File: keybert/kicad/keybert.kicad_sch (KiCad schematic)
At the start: 52 parts, among them SW0 MX-NoLED, SW1 MX-NoLED, SW10 MX-NoLED, SW11 MX-NoLED, SW12 MX-NoLED, SW13 MX-NoLED, SW14 MX-NoLED, SW15 MX-NoLED, SW16 MX-NoLED, SW17 MX-NoLED, SW18 MX-NoLED, SW19 MX-NoLED, SW2 MX-NoLED, SW20 MX-NoLED, SW21 MX-NoLED, SW22 MX-NoLED, SW3 MX-NoLED, SW4 MX-NoLED, SW5 MX-NoLED, SW6 MX-NoLED, SW7 MX-NoLED, SW8 MX-NoLED, SW9 MX-NoLED, U0 ProMicro

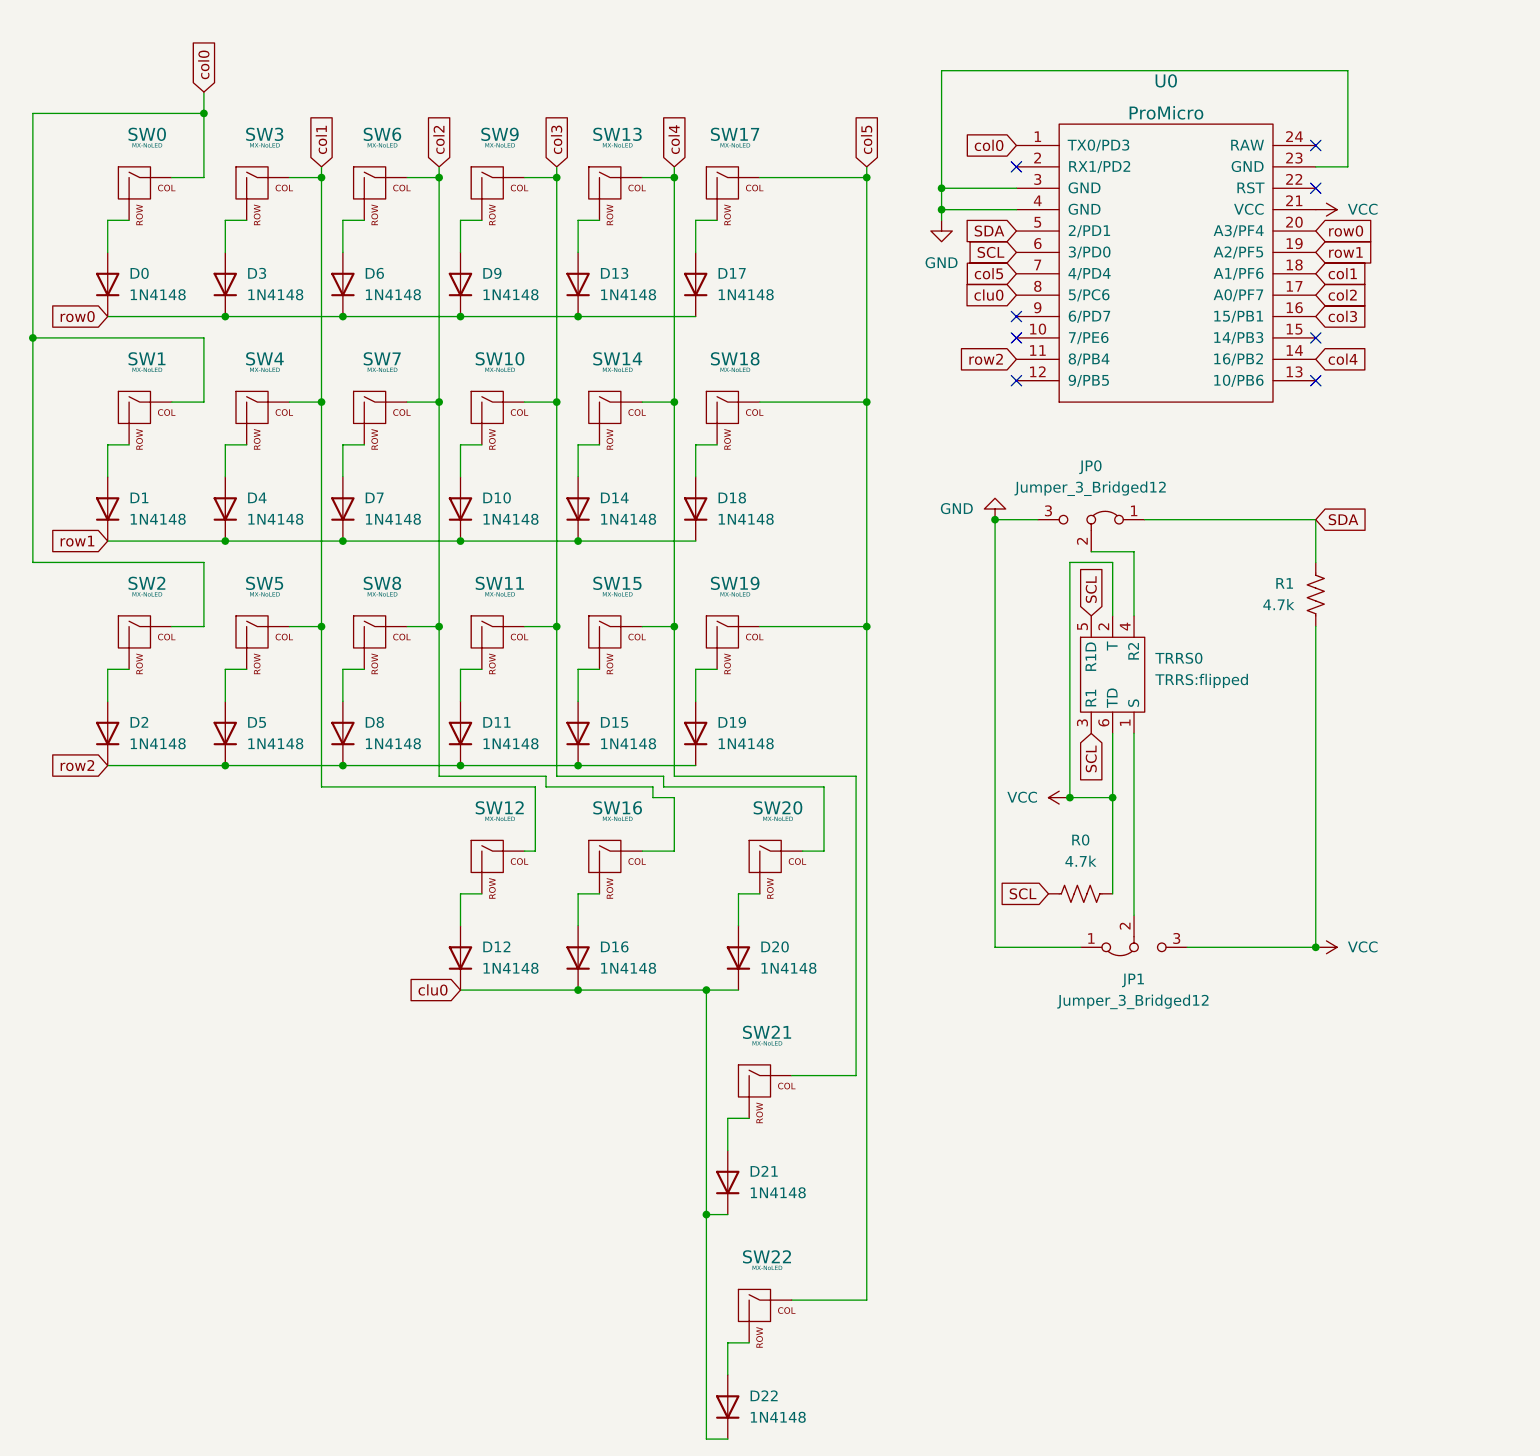
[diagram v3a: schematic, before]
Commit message: feat: remade parametric model of switch plate
I'm going to have a friend help me get it sorted out why the parameters
are coming out so under constrained
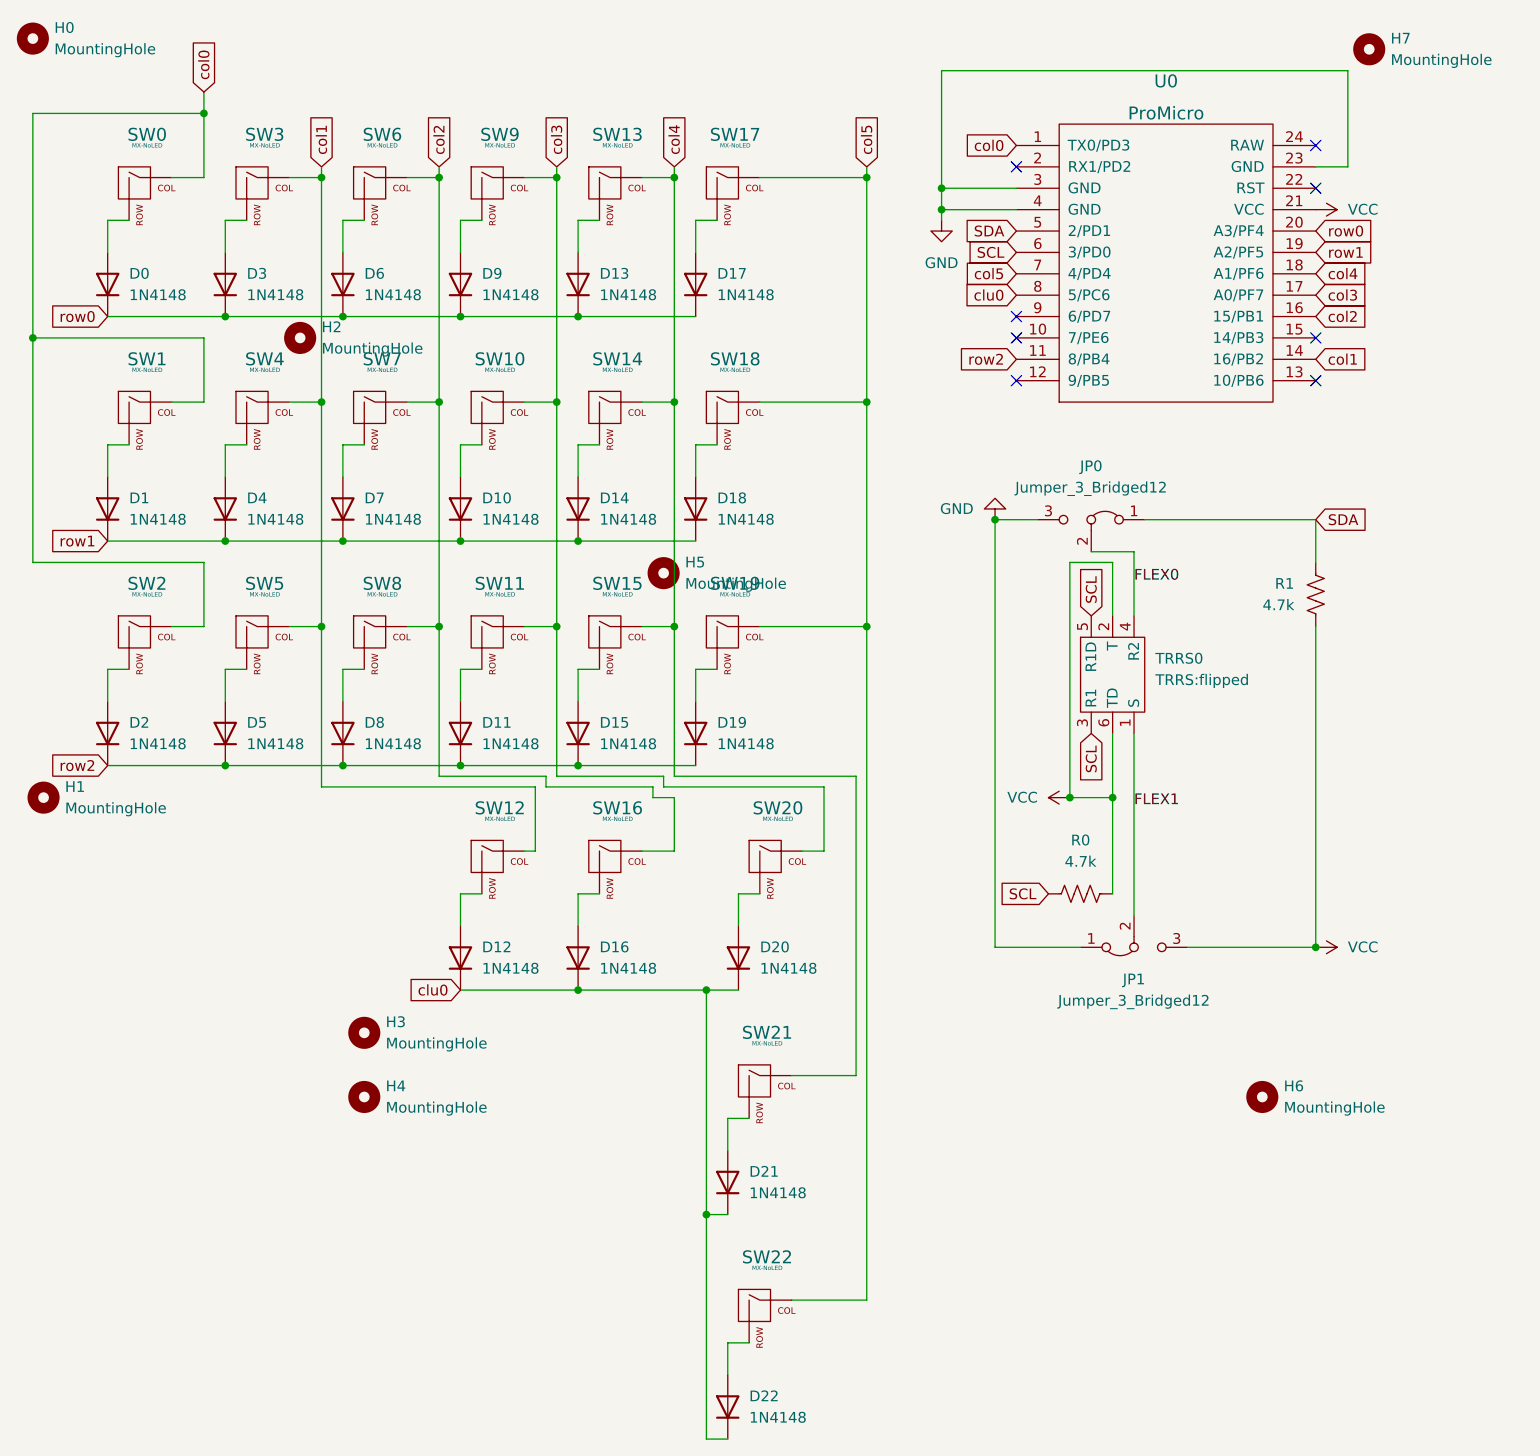
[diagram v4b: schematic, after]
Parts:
- added H0, H1, H2, H3, H4, H5, H6, H7: MountingHole, symbol Mechanical:MountingHole
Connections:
- net col1: now also U0.14 (16/PB2); no longer U0.18 (A1/PF6)
- net col2: now also U0.16 (15/PB1); no longer U0.17 (A0/PF7)
- net col3: now also U0.17 (A0/PF7); no longer U0.16 (15/PB1)
- net col4: now also U0.18 (A1/PF6); no longer U0.14 (16/PB2)
- net FLEX0: now reaches JP0.2 (C), TRRS0.4 (R2)
- net FLEX1: now reaches JP1.2 (C), TRRS0.1 (S)
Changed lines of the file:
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@@
     (stroke (width 0) (type default) (color 0 0 0 0))
+  )
+  (label "FLEX1" (at 144.78 105.41 0)
+    (effects (font (size 1.27 1.27)) (justify left bottom))
+  )
+  (label "FLEX0" (at 144.78 78.74 0)
+    (effects (font (size 1.27 1.27)) (justify left bottom))
   )
   (global_label "row2" (shape input) (at 130.81 52.07 180) (fields_autoplaced)
@@
     )
   )
-  (global_label "col1" (shape input) (at 166.37 41.91 0) (fields_autoplaced)
+  (global_label "col4" (shape input) (at 166.37 41.91 0) (fields_autoplaced)
     (effects (font (size 1.27 1.27)) (justify left))
     (property "Intersheet References" "${INTERSHEET_REFS}" (id 0) (at 172.8955 41.8306 0)
@@
     )
   )
-  (global_label "col3" (shape input) (at 166.37 46.99 0) (fields_autoplaced)
+  (global_label "col2" (shape input) (at 166.37 46.99 0) (fields_autoplaced)
     (effects (font (size 1.27 1.27)) (justify left))
     (property "Intersheet References" "${INTERSHEET_REFS}" (id 0) (at 172.8955 46.9106 0)
@@
     )
   )
-  (global_label "col4" (shape input) (at 166.37 52.07 0) (fields_autoplaced)
+  (global_label "col1" (shape input) (at 166.37 52.07 0) (fields_autoplaced)
     (effects (font (size 1.27 1.27)) (justify left))
     (property "Intersheet References" "${INTERSHEET_REFS}" (id 0) (at 172.8955 51.9906 0)
@@
     )
   )
-  (global_label "col2" (shape input) (at 166.37 44.45 0) (fields_autoplaced)
+  (global_label "col3" (shape input) (at 166.37 44.45 0) (fields_autoplaced)
     (effects (font (size 1.27 1.27)) (justify left))
     (property "Intersheet References" "${INTERSHEET_REFS}" (id 0) (at 172.8955 44.3706 0)
@@
     (pin "1")
     (pin "2")
+  )
+  (symbol (lib_id "Mechanical:MountingHole") (at 172.72 15.24 0) (unit 1)
+    (in_bom yes) (on_board yes) (fields_autoplaced)
+    (property "Reference" "H7" (id 0) (at 175.26 13.9699 0)
+      (effects (font (size 1.27 1.27)) (justify left))
+    )
+    (property "Value" "MountingHole" (id 1) (at 175.26 16.5099 0)
+      (effects (font (size 1.27 1.27)) (justify left))
+    )
+    (property "Footprint" "" (id 2) (at 172.72 15.24 0)
+      (effects (font (size 1.27 1.27)) hide)
+    )
+    (property "Datasheet" "~" (id 3) (at 172.72 15.24 0)
+      (effects (font (size 1.27 1.27)) hide)
+    )
+  )
+  (symbol (lib_id "Mechanical:MountingHole") (at 15.24 104.14 0) (unit 1)
+    (in_bom yes) (on_board yes) (fields_autoplaced)
+    (property "Reference" "H1" (id 0) (at 17.78 102.8699 0)
+      (effects (font (size 1.27 1.27)) (justify left))
+    )
+    (property "Value" "MountingHole" (id 1) (at 17.78 105.4099 0)
+      (effects (font (size 1.27 1.27)) (justify left))
+    )
+    (property "Footprint" "" (id 2) (at 15.24 104.14 0)
+      (effects (font (size 1.27 1.27)) hide)
+    )
+    (property "Datasheet" "~" (id 3) (at 15.24 104.14 0)
+      (effects (font (size 1.27 1.27)) hide)
+    )
   )
   (symbol (lib_id "MX_Alps_Hybrid:MX-NoLED") (at 54.61 85.09 0) (unit 1)
@@
     (pin "2")
   )
+  (symbol (lib_id "Mechanical:MountingHole") (at 13.97 13.97 0) (unit 1)
+    (in_bom yes) (on_board yes) (fields_autoplaced)
+    (property "Reference" "H0" (id 0) (at 16.51 12.6999 0)
+      (effects (font (size 1.27 1.27)) (justify left))
+    )
+    (property "Value" "MountingHole" (id 1) (at 16.51 15.2399 0)
+      (effects (font (size 1.27 1.27)) (justify left))
+    )
+    (property "Footprint" "" (id 2) (at 13.97 13.97 0)
+      (effects (font (size 1.27 1.27)) hide)
+    )
+    (property "Datasheet" "~" (id 3) (at 13.97 13.97 0)
+      (effects (font (size 1.27 1.27)) hide)
+    )
+  )
   (symbol (lib_id "power:VCC") (at 166.37 34.29 270) (mirror x) (unit 1)
     (in_bom yes) (on_board yes) (fields_autoplaced)
@@
     (pin "1")
     (pin "2")
+  )
+  (symbol (lib_id "Mechanical:MountingHole") (at 53.34 132.08 0) (unit 1)
+    (in_bom yes) (on_board yes) (fields_autoplaced)
+    (property "Reference" "H3" (id 0) (at 55.88 130.8099 0)
+      (effects (font (size 1.27 1.27)) (justify left))
+    )
+    (property "Value" "MountingHole" (id 1) (at 55.88 133.3499 0)
+      (effects (font (size 1.27 1.27)) (justify left))
+    )
+    (property "Footprint" "" (id 2) (at 53.34 132.08 0)
+      (effects (font (size 1.27 1.27)) hide)
+    )
+    (property "Datasheet" "~" (id 3) (at 53.34 132.08 0)
+      (effects (font (size 1.27 1.27)) hide)
+    )
   )
   (symbol (lib_id "power:GND") (at 128.27 71.12 0) (mirror x) (unit 1)
@@
     (pin "2")
   )
+  (symbol (lib_id "Mechanical:MountingHole") (at 53.34 139.7 0) (unit 1)
+    (in_bom yes) (on_board yes) (fields_autoplaced)
+    (property "Reference" "H4" (id 0) (at 55.88 138.4299 0)
+      (effects (font (size 1.27 1.27)) (justify left))
+    )
+    (property "Value" "MountingHole" (id 1) (at 55.88 140.9699 0)
+      (effects (font (size 1.27 1.27)) (justify left))
+    )
+    (property "Footprint" "" (id 2) (at 53.34 139.7 0)
+      (effects (font (size 1.27 1.27)) hide)
+    )
+    (property "Datasheet" "~" (id 3) (at 53.34 139.7 0)
+      (effects (font (size 1.27 1.27)) hide)
+    )
+  )
   (symbol (lib_id "Diode:1N4148") (at 50.8 69.85 90) (unit 1)
     (in_bom yes) (on_board yes) (fields_autoplaced)
@@
     (pin "2")
   )
+  (symbol (lib_id "Mechanical:MountingHole") (at 88.9 77.47 0) (unit 1)
+    (in_bom yes) (on_board yes) (fields_autoplaced)
+    (property "Reference" "H5" (id 0) (at 91.44 76.1999 0)
+      (effects (font (size 1.27 1.27)) (justify left))
+    )
+    (property "Value" "MountingHole" (id 1) (at 91.44 78.7399 0)
+      (effects (font (size 1.27 1.27)) (justify left))
+    )
+    (property "Footprint" "" (id 2) (at 88.9 77.47 0)
+      (effects (font (size 1.27 1.27)) hide)
+    )
+    (property "Datasheet" "~" (id 3) (at 88.9 77.47 0)
+      (effects (font (size 1.27 1.27)) hide)
+    )
+  )
   (symbol (lib_id "Diode:1N4148") (at 36.83 43.18 90) (unit 1)
     (in_bom yes) (on_board yes) (fields_autoplaced)
@@
     (pin "1")
     (pin "2")
+  )
+  (symbol (lib_id "Mechanical:MountingHole") (at 45.72 49.53 0) (unit 1)
+    (in_bom yes) (on_board yes) (fields_autoplaced)
+    (property "Reference" "H2" (id 0) (at 48.26 48.2599 0)
+      (effects (font (size 1.27 1.27)) (justify left))
+    )
+    (property "Value" "MountingHole" (id 1) (at 48.26 50.7999 0)
+      (effects (font (size 1.27 1.27)) (justify left))
+    )
+    (property "Footprint" "" (id 2) (at 45.72 49.53 0)
+      (effects (font (size 1.27 1.27)) hide)
+    )
+    (property "Datasheet" "~" (id 3) (at 45.72 49.53 0)
+      (effects (font (size 1.27 1.27)) hide)
+    )
   )
   (symbol (lib_id "MX_Alps_Hybrid:MX-NoLED") (at 96.52 85.09 0) (unit 1)
@@
     (pin "2")
   )
+  (symbol (lib_id "Mechanical:MountingHole") (at 160.02 139.7 0) (unit 1)
+    (in_bom yes) (on_board yes) (fields_autoplaced)
+    (property "Reference" "H6" (id 0) (at 162.56 138.4299 0)
+      (effects (font (size 1.27 1.27)) (justify left))
+    )
+    (property "Value" "MountingHole" (id 1) (at 162.56 140.9699 0)
+      (effects (font (size 1.27 1.27)) (justify left))
+    )
+    (property "Footprint" "" (id 2) (at 160.02 139.7 0)
+      (effects (font (size 1.27 1.27)) hide)
+    )
+    (property "Datasheet" "~" (id 3) (at 160.02 139.7 0)
+      (effects (font (size 1.27 1.27)) hide)
+    )
+  )
   (symbol (lib_id "MX_Alps_Hybrid:MX-NoLED") (at 101.6 111.76 0) (unit 1)
     (in_bom yes) (on_board yes) (fields_autoplaced)
@@
       (reference "D22") (unit 1) (value "1N4148") (footprint "Keebio-Parts:Diode")
     )
+    (path "/489a4b6c-61c0-414e-83ad-d85967ecde03"
+      (reference "H0") (unit 1) (value "MountingHole") (footprint "")
+    )
+    (path "/236278e9-fdde-4742-82f9-7df0de3fc2a7"
+      (reference "H1") (unit 1) (value "MountingHole") (footprint "")
+    )
+    (path "/e47dcbe1-febf-4bd4-b703-aca7cc01f6fb"
+      (reference "H2") (unit 1) (value "MountingHole") (footprint "")
+    )
+    (path "/5d19d2d2-3a36-4137-842d-5d26104261f5"
+      (reference "H3") (unit 1) (value "MountingHole") (footprint "")
+    )
+    (path "/7ca6e89e-ee90-46a4-8403-401b79c69bfe"
+      (reference "H4") (unit 1) (value "MountingHole") (footprint "")
+    )
+    (path "/cfb72d3f-b4ef-4d11-ac0f-7afdfca579e2"
+      (reference "H5") (unit 1) (value "MountingHole") (footprint "")
+    )
+    (path "/f9e12466-0f35-4cc2-961f-0abbc58f469a"
+      (reference "H6") (unit 1) (value "MountingHole") (footprint "")
+    )
+    (path "/1425dbc6-e380-423b-a297-c62c53953374"
+      (reference "H7") (unit 1) (value "MountingHole") (footprint "")
+    )
     (path "/80fc0860-4643-44f6-9ea9-9afd93cea867"
